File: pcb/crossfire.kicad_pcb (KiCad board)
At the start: 4 copper layers, 100 x 80 mm, 148 parts, among them J1 SWD+UART, J2 USB_A, J3 USB_A, J4 USB_A, J5 USB_A, J6 USB-C data, J7 1S LiPo, J8 USB-C power, Q1 Q_Dual_NMOS_S1G1S2G2D2D2D1D1, Q2 Q_Dual_NMOS_S1G1S2G2D2D2D1D1, Q3 Q_Dual_NMOS_S1G1S2G2D2D2D1D1, SW1 BOOT, SW2 RESET, SW3 USER, U1 RP2350A, U10 TPS2065C, U11 USBLC6-2SC6, U12 USBLC6-2SC6, U13 BQ25798, U14 TPS63060, U15 TPS61089, U16 HUSB238, U17 RM2, U2 W25Q128JVS, U3 USB2514B, U4 TPS2065C, U5 USBLC6-2SC6, U6 TPS2065C, U7 USBLC6-2SC6, U8 TPS2065C, U9 USBLC6-2SC6, Y1 12MHz, Y2 24MHz

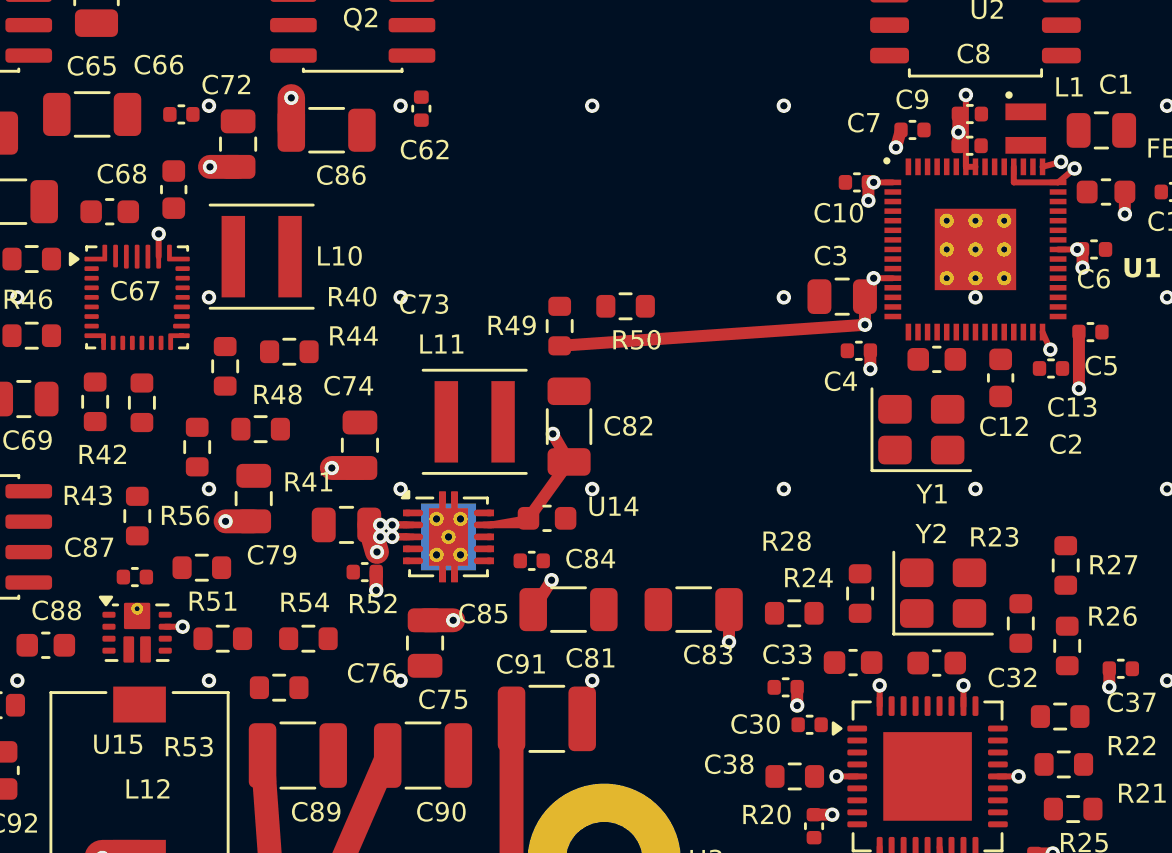
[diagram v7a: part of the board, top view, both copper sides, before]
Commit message: route what can be verified, and keep only that
The plan was to route by script the nets where a rule exists and can be checked -- the twelve data
pairs as pairs, both crystals, the converters' switch nodes -- and leave the rest to be routed by
hand. The division was right; the expectation of the tool was not. Three short routes survive, and
this records why, because the attempt is what found the placement fault that mattered far more.

A maze search over the two outer layers, with a pair searched as one object: the state is the
centreline between the two tracks, each offset half the pair pitch to its own side, so the two come
out parallel by construction rather than routed one after the other, which is two tracks and not a
pair. It routed. It did not agree with the rules check, and each disagreement found revealed another.

A pad's own cells were blocked, because the centre of a pin on a 0.4mm package is within clearance of
the pins either side -- true, and irrelevant, since that copper is already there and a track inside
its own pad adds no problem the pad does not already have. A clearance halo was painted as a grown
bounding box, which blocks a rectangle's diagonals by root two times the clearance, sealing every
fine-pitch escape. A pair cannot leave fine pitch AS a pair: it needs a millimetre of width and there
is none between 0.4mm pins, so it fans out as two tracks and comes together outside the part. And the
fan-out itself was drawn without checking anything, which was thirty-nine shorts in one run.

After all that the checker still rejected most of the output, so the only safe rule was applied: keep
what the authority verifies and take the rest off. The rules check is run, every net named in a
violation is read out of it, and every track on a routed net named there is removed. Three routes
remain, all short and all verified -- the core regulator's switch node at 0.9mm, the boost's
bootstrap at 1.8mm, the hub's crystal input at 4.0mm.

A fourth was removed by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
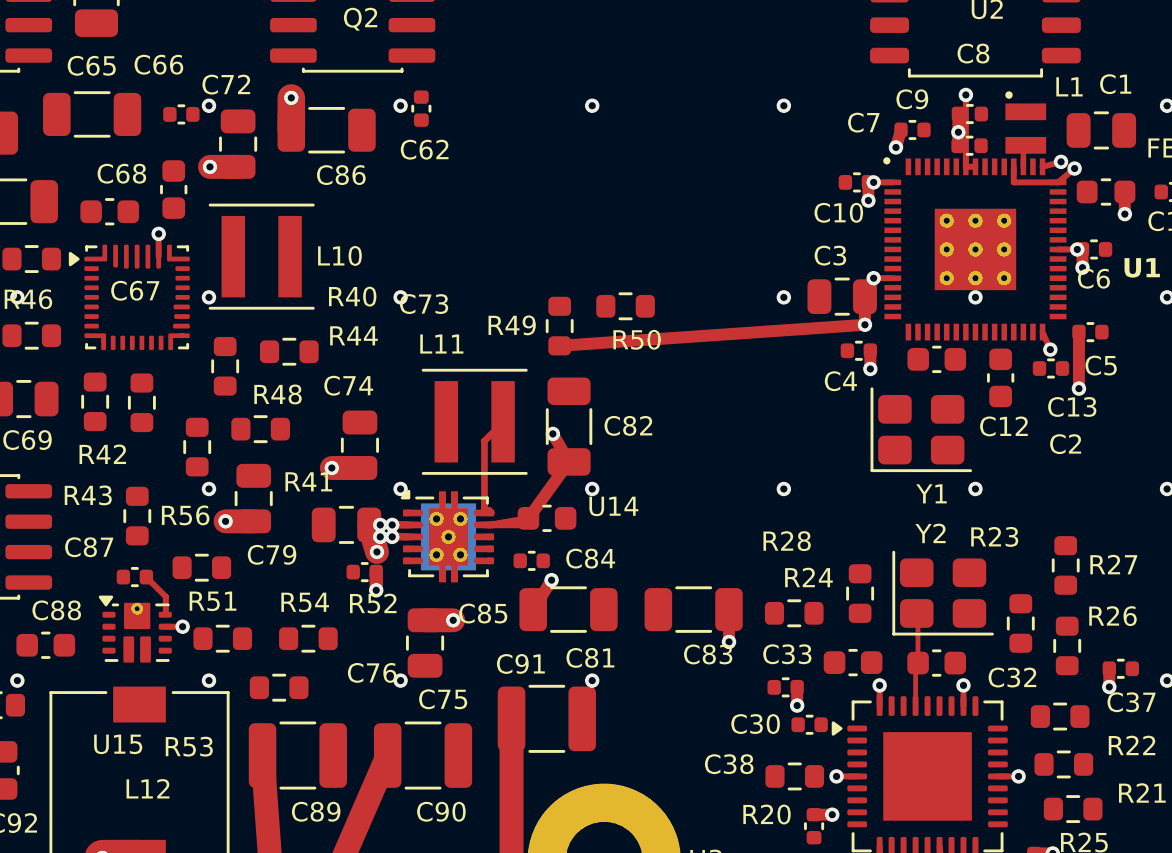
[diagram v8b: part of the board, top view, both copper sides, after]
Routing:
- net Net-(U14-L2): track 0.00 -> 4.60 mm
- net Net-(U3-XTALIN/CLKIN): track 0.00 -> 3.98 mm
- net Net-(U15-BOOT): track 0.00 -> 1.83 mm
- net Net-(U1-VREG_LX): track 0.00 -> 0.94 mm
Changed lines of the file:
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@@
+	)
+	(segment
+		(start 49.6 49.3)
+		(end 49.5 49.2)
+		(width 0.2)
+		(layer "F.Cu")
+		(net "Net-(U3-XTALIN{slash}CLKIN)")
+	)
+	(segment
+		(start 49.6 51.3)
+		(end 49.6 49.3)
+		(width 0.2)
+		(layer "F.Cu")
+		(net "Net-(U3-XTALIN{slash}CLKIN)")
+	)
+	(segment
+		(start 49.5 53.1)
+		(end 49.5 51.4)
+		(width 0.2)
+		(layer "F.Cu")
+		(net "Net-(U3-XTALIN{slash}CLKIN)")
+	)
+	(segment
+		(start 49.5 51.4)
+		(end 49.6 51.3)
+		(width 0.2)
+		(layer "F.Cu")
+		(net "Net-(U3-XTALIN{slash}CLKIN)")
 	)
 	(segment
@@
 		(net "/power/VSYS")
 	)
+	(segment
+		(start 54 30.6)
+		(end 54 29.8)
+		(width 0.23)
+		(layer "F.Cu")
+		(net "Net-(U1-VREG_LX)")
+	)
+	(segment
+		(start 54 29.8)
+		(end 54.1 29.7)
+		(width 0.23)
+		(layer "F.Cu")
+		(net "Net-(U1-VREG_LX)")
+	)
+	(segment
+		(start 31.5 42)
+		(end 32.3 41.2)
+		(width 0.28)
+		(layer "F.Cu")
+		(net "Net-(U14-L2)")
+	)
+	(segment
+		(start 31.6 44.9)
+		(end 31.5 44.8)
+		(width 0.28)
+		(layer "F.Cu")
+		(net "Net-(U14-L2)")
+	)
+	(segment
+		(start 31.7 44.9)
+		(end 31.6 44.9)
+		(width 0.28)
+		(layer "F.Cu")
+		(net "Net-(U14-L2)")
+	)
+	(segment
+		(start 31.8 45)
+		(end 31.7 44.9)
+		(width 0.28)
+		(layer "F.Cu")
+		(net "Net-(U14-L2)")
+	)
+	(segment
+		(start 31.475 45)
+		(end 31.76 45)
+		(width 0.25)
+		(layer "F.Cu")
+		(net "Net-(U14-L2)")
+	)
+	(segment
+		(start 31.5 44.8)
+		(end 31.5 42)
+		(width 0.28)
+		(layer "F.Cu")
+		(net "Net-(U14-L2)")
+	)
+	(segment
+		(start 18.2 48.5)
+		(end 17.4 47.7)
+		(width 0.25)
+		(layer "F.Cu")
+		(net "Net-(U15-BOOT)")
+	)
+	(segment
+		(start 18.2 49.2)
+		(end 18.2 48.5)
+		(width 0.25)
+		(layer "F.Cu")
+		(net "Net-(U15-BOOT)")
+	)
 	(zone
